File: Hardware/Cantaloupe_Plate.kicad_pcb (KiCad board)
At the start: 2 copper layers, 142.1 x 117 mm, 36 parts, among them SW1 MX, SW10 MX, SW11 MX, SW12 MX, SW13 MX, SW14 MX, SW15 MX, SW16 MX, SW17 MX, SW18 MX, SW19 MX, SW2 MX, SW20 MX, SW21 MX, SW22 MX, SW23 MX, SW24 MX, SW25 MX, SW26 MX, SW27 MX, SW28 MX, SW29 MX, SW3 MX, SW30 MX, SW31 MX, SW4 MX, SW5 MX, SW6 MX, SW7 MX, SW8 MX, SW9 MX

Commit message: Updated to V1.2
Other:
- outline, holes or cut-outs redrawn

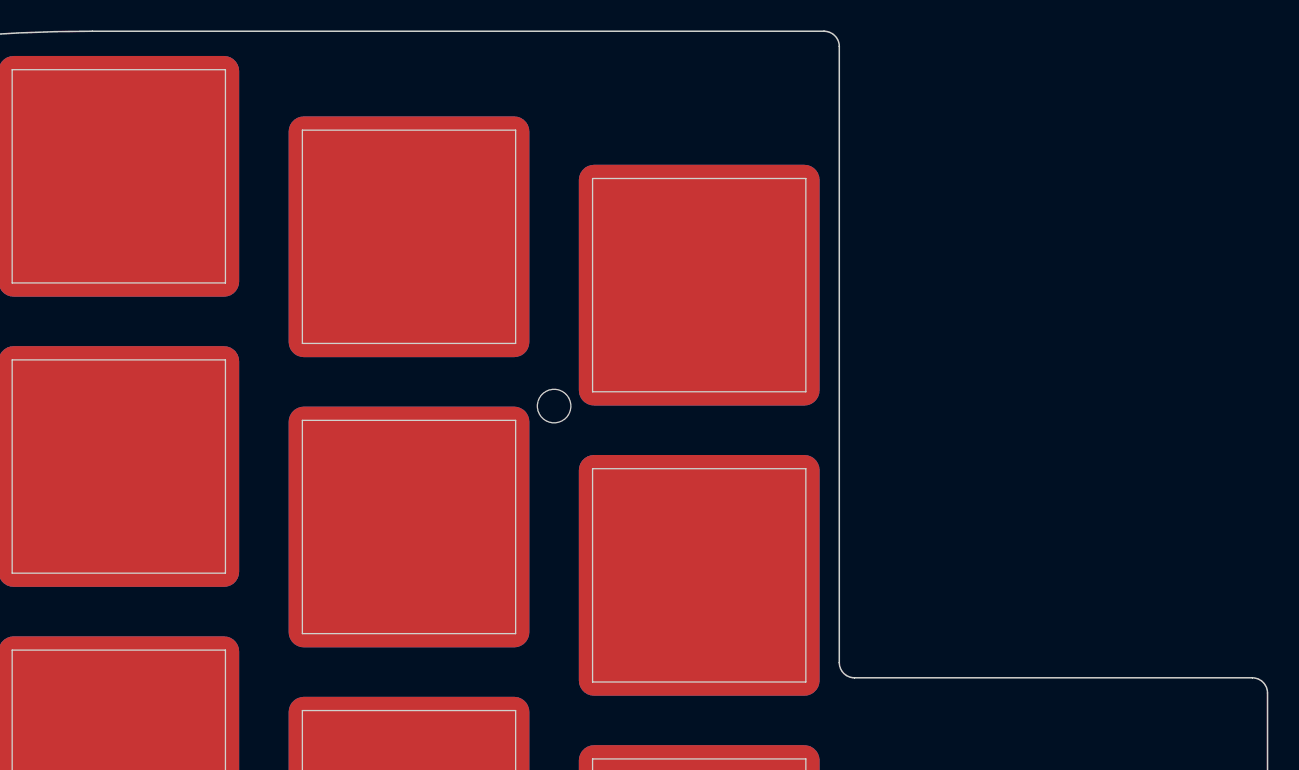
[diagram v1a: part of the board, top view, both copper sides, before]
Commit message: Changed USB C connector to normal from mid-mount
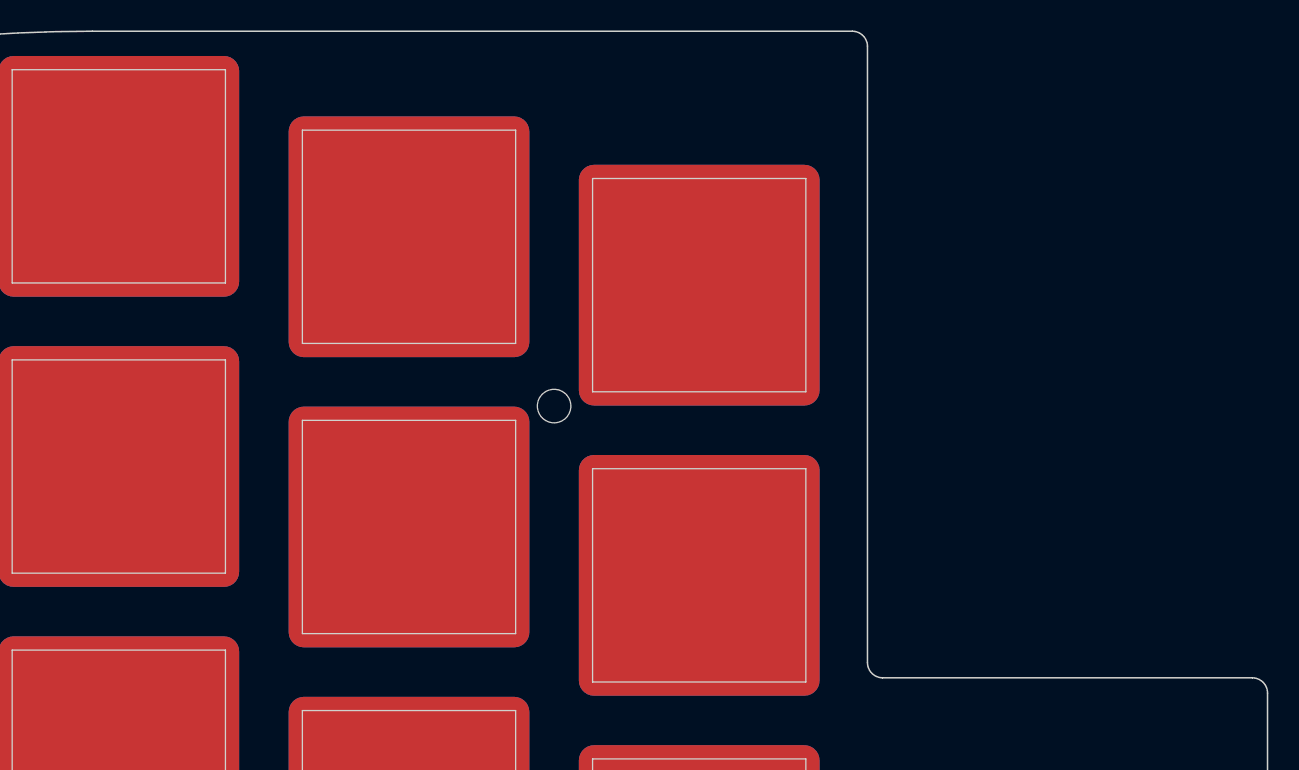
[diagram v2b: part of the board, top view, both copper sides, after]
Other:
- outline, holes or cut-outs redrawn
